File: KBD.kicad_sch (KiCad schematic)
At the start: 41 parts, among them SW1 SW_Push, SW10 SW_Push, SW11 SW_Push, SW12 SW_Push, SW13 SW_Push, SW14 SW_Push, SW15 SW_Push, SW16 SW_Push, SW17 SW_Push, SW18 SW_Push, SW2 SW_Push, SW3 SW_Push, SW4 SW_Push, SW5 SW_Push, SW6 SW_Push, SW7 SW_Push, SW8 SW_Push, SW9 SW_Push, U1 SeeeduinoXIAO

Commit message: aaaaaaa
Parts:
- removed R1, R2, R3, R4: 10k, Resistor_SMD:R_0805_2012Metric_Pad1.20x1.40mm_HandSolder, symbol Device:R
- SW1, SW10, SW11, SW12, SW13, SW14, SW15, SW16, SW17, SW18, SW2, SW3, SW4, SW5, SW6, SW7, SW8, SW9: footprint CustomKeyboard:Choc_reversible -> Split_footprints:Choc_reversible_17mmOutline
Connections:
- net Row_1: now also D1.1 (K), D13.1 (K), D16.1 (K), D5.1 (K), D9.1 (K)
- net Row_2: now also D10.1 (K), D14.1 (K), D17.1 (K), D2.1 (K), D6.1 (K)
- net Row_3: now also D11.1 (K), D15.1 (K), D18.1 (K), D3.1 (K), D7.1 (K)
- net Row_4: now also D12.1 (K), D4.1 (K), D8.1 (K)

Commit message: bbbbb
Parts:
- renumbered D17 to D10, D3 to D11, D7 to D12, D11 to D13, D15 to D14, D18 to D15, D4 to D16, D8 to D17, D12 to D18, D5 to D2, D9 to D3, D13 to D4, D16 to D5, D2 to D6, D6 to D7, D10 to D8, D14 to D9, SW17 to SW10, SW3 to SW11, SW7 to SW12, SW11 to SW13, SW15 to SW14, SW18 to SW15, SW4 to SW16, SW8 to SW17, SW12 to SW18, SW5 to SW2, SW9 to SW3, SW13 to SW4, SW16 to SW5, SW2 to SW6, SW6 to SW7, SW10 to SW8, SW14 to SW9

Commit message: bbbbbb1
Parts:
- added D19: WS2812B, LED_SMD:LED_WS2812B_PLCC4_5.0x5.0mm_P3.2mm, symbol LED:WS2812B
- added J1, J2: Conn_01x07, Connector_Hirose:Hirose_DF13-07P-1.25DS_1x07_P1.25mm_Horizontal, symbol Connector_Generic:Conn_01x07
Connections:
- net Column_1: now also J1.6 (Pin_6); no longer U1.6 (PA9_A5_D5_SCL)
- net Column_2: now also J2.1 (Pin_1); no longer U1.7 (PB08_A6_D6_TX)
- net Column_3: now also J2.2 (Pin_2); no longer U1.8 (PB09_A7_D7_RX)
- net Column_4: now also J2.3 (Pin_3); no longer U1.9 (PA7_A8_D8_SCK)
- net Column_5: now also J2.4 (Pin_4); no longer U1.10 (PA5_A9_D9_MISO)
- net Row_1: now also J1.1 (Pin_1); no longer U1.1 (PA02_A0_D0)
- net Row_2: now also J1.2 (Pin_2); no longer U1.2 (PA4_A1_D1)
- net Row_3: now also J1.3 (Pin_3); no longer U1.3 (PA10_A2_D2)
- net Row_4: now also J1.4 (Pin_4); no longer U1.4 (PA11_A3_D3)
- new net 0V: D19.3 (VSS), J2.6 (Pin_6)
- new net 5V: D19.1 (VDD), J2.7 (Pin_7)
- new net Led_In: D19.4 (DIN), J1.5 (Pin_5)
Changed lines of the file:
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@@
     (stroke (width 0) (type default))
   )
-  (global_label "Column_1" (shape output) (at 40.64 74.93 180) (fields_autoplaced)
-    (effects (font (size 1.27 1.27)) (justify right))
-    (property "Intersheetrefs" "${INTERSHEET_REFS}" (at 28.974 74.8506 0)
-      (effects (font (size 1.27 1.27)) (justify right) hide)
-    )
-  )
-  (global_label "Row_1" (shape input) (at 40.64 55.88 180) (fields_autoplaced)
-    (effects (font (size 1.27 1.27)) (justify right))
-    (property "Intersheetrefs" "${INTERSHEET_REFS}" (at 32.3002 55.8006 0)
+  (global_label "5V" (shape input) (at 55.88 130.81 90) (fields_autoplaced)
+    (effects (font (size 1.27 1.27)) (justify left))
+    (property "Intersheetrefs" "${INTERSHEET_REFS}" (at 55.88 125.6061 90)
+      (effects (font (size 1.27 1.27)) (justify left) hide)
+    )
+  )
+  (global_label "0V" (shape input) (at 71.12 107.95 0) (fields_autoplaced)
+    (effects (font (size 1.27 1.27)) (justify left))
+    (property "Intersheetrefs" "${INTERSHEET_REFS}" (at 76.3239 107.95 0)
+      (effects (font (size 1.27 1.27)) (justify left) hide)
+    )
+  )
+  (global_label "Column_1" (shape output) (at 43.18 118.11 180) (fields_autoplaced)
+    (effects (font (size 1.27 1.27)) (justify right))
+    (property "Intersheetrefs" "${INTERSHEET_REFS}" (at 31.514 118.0306 0)
+      (effects (font (size 1.27 1.27)) (justify right) hide)
+    )
+  )
+  (global_label "Row_1" (shape input) (at 43.18 105.41 180) (fields_autoplaced)
+    (effects (font (size 1.27 1.27)) (justify right))
+    (property "Intersheetrefs" "${INTERSHEET_REFS}" (at 34.8402 105.3306 0)
       (effects (font (size 1.27 1.27)) (justify right) hide)
     )
@@
     )
   )
-  (global_label "Row_2" (shape input) (at 40.64 59.69 180) (fields_autoplaced)
-    (effects (font (size 1.27 1.27)) (justify right))
-    (property "Intersheetrefs" "${INTERSHEET_REFS}" (at 32.3002 59.6106 0)
-      (effects (font (size 1.27 1.27)) (justify right) hide)
-    )
-  )
-  (global_label "Column_4" (shape output) (at 82.55 74.93 0) (fields_autoplaced)
-    (effects (font (size 1.27 1.27)) (justify left))
-    (property "Intersheetrefs" "${INTERSHEET_REFS}" (at 94.216 74.8506 0)
-      (effects (font (size 1.27 1.27)) (justify left) hide)
+  (global_label "Row_2" (shape input) (at 43.18 107.95 180) (fields_autoplaced)
+    (effects (font (size 1.27 1.27)) (justify right))
+    (property "Intersheetrefs" "${INTERSHEET_REFS}" (at 34.8402 107.8706 0)
+      (effects (font (size 1.27 1.27)) (justify right) hide)
+    )
+  )
+  (global_label "Column_4" (shape output) (at 71.12 115.57 0) (fields_autoplaced)
+    (effects (font (size 1.27 1.27)) (justify left))
+    (property "Intersheetrefs" "${INTERSHEET_REFS}" (at 82.786 115.4906 0)
+      (effects (font (size 1.27 1.27)) (justify left) hide)
+    )
+  )
+  (global_label "Led_In" (shape input) (at 43.18 115.57 180) (fields_autoplaced)
+    (effects (font (size 1.27 1.27)) (justify right))
+    (property "Intersheetrefs" "${INTERSHEET_REFS}" (at 34.2871 115.57 0)
+      (effects (font (size 1.27 1.27)) (justify right) hide)
     )
   )
@@
     )
   )
-  (global_label "Row_3" (shape input) (at 40.64 63.5 180) (fields_autoplaced)
-    (effects (font (size 1.27 1.27)) (justify right))
-    (property "Intersheetrefs" "${INTERSHEET_REFS}" (at 32.3002 63.4206 0)
-      (effects (font (size 1.27 1.27)) (justify right) hide)
-    )
-  )
-  (global_label "Column_2" (shape output) (at 40.64 78.74 180) (fields_autoplaced)
-    (effects (font (size 1.27 1.27)) (justify right))
-    (property "Intersheetrefs" "${INTERSHEET_REFS}" (at 28.974 78.6606 0)
-      (effects (font (size 1.27 1.27)) (justify right) hide)
-    )
-  )
-  (global_label "Row_4" (shape input) (at 40.64 67.31 180) (fields_autoplaced)
-    (effects (font (size 1.27 1.27)) (justify right))
-    (property "Intersheetrefs" "${INTERSHEET_REFS}" (at 32.3002 67.2306 0)
-      (effects (font (size 1.27 1.27)) (justify right) hide)
-    )
-  )
-  (global_label "Column_5" (shape output) (at 82.55 71.12 0) (fields_autoplaced)
-    (effects (font (size 1.27 1.27)) (justify left))
-    (property "Intersheetrefs" "${INTERSHEET_REFS}" (at 94.216 71.0406 0)
+  (global_label "Row_3" (shape input) (at 43.18 110.49 180) (fields_autoplaced)
+    (effects (font (size 1.27 1.27)) (justify right))
+    (property "Intersheetrefs" "${INTERSHEET_REFS}" (at 34.8402 110.4106 0)
+      (effects (font (size 1.27 1.27)) (justify right) hide)
+    )
+  )
+  (global_label "Column_2" (shape output) (at 71.12 120.65 0) (fields_autoplaced)
+    (effects (font (size 1.27 1.27)) (justify left))
+    (property "Intersheetrefs" "${INTERSHEET_REFS}" (at 83.2784 120.65 0)
+      (effects (font (size 1.27 1.27)) (justify left) hide)
+    )
+  )
+  (global_label "Row_4" (shape input) (at 43.18 113.03 180) (fields_autoplaced)
+    (effects (font (size 1.27 1.27)) (justify right))
+    (property "Intersheetrefs" "${INTERSHEET_REFS}" (at 34.8402 112.9506 0)
+      (effects (font (size 1.27 1.27)) (justify right) hide)
+    )
+  )
+  (global_label "Column_5" (shape output) (at 71.12 113.03 0) (fields_autoplaced)
+    (effects (font (size 1.27 1.27)) (justify left))
+    (property "Intersheetrefs" "${INTERSHEET_REFS}" (at 82.786 112.9506 0)
       (effects (font (size 1.27 1.27)) (justify left) hide)
     )
@@
     )
   )
-  (global_label "Column_3" (shape output) (at 82.55 78.74 0) (fields_autoplaced)
-    (effects (font (size 1.27 1.27)) (justify left))
-    (property "Intersheetrefs" "${INTERSHEET_REFS}" (at 94.216 78.6606 0)
+  (global_label "Column_3" (shape output) (at 71.12 118.11 0) (fields_autoplaced)
+    (effects (font (size 1.27 1.27)) (justify left))
+    (property "Intersheetrefs" "${INTERSHEET_REFS}" (at 82.786 118.0306 0)
       (effects (font (size 1.27 1.27)) (justify left) hide)
     )
@@
     )
   )
+  (global_label "5V" (shape input) (at 71.12 105.41 0) (fields_autoplaced)
+    (effects (font (size 1.27 1.27)) (justify left))
+    (property "Intersheetrefs" "${INTERSHEET_REFS}" (at 76.3239 105.41 0)
+      (effects (font (size 1.27 1.27)) (justify left) hide)
+    )
+  )
+  (global_label "0V" (shape input) (at 55.88 146.05 270) (fields_autoplaced)
+    (effects (font (size 1.27 1.27)) (justify right))
+    (property "Intersheetrefs" "${INTERSHEET_REFS}" (at 55.88 151.2539 90)
+      (effects (font (size 1.27 1.27)) (justify right) hide)
+    )
+  )
   (global_label "Column_2" (shape output) (at 154.94 62.23 90) (fields_autoplaced)
     (effects (font (size 1.27 1.27)) (justify left))
     (property "Intersheetrefs" "${INTERSHEET_REFS}" (at 154.8606 50.564 90)
       (effects (font (size 1.27 1.27)) (justify left) hide)
+    )
+  )
+  (global_label "Led_In" (shape input) (at 48.26 138.43 180) (fields_autoplaced)
+    (effects (font (size 1.27 1.27)) (justify right))
+    (property "Intersheetrefs" "${INTERSHEET_REFS}" (at 39.3671 138.43 0)
+      (effects (font (size 1.27 1.27)) (justify right) hide)
     )
   )
@@
     )
   )
+  (symbol (lib_id "LED:WS2812B") (at 55.88 138.43 0) (unit 1)
+    (in_bom yes) (on_board yes) (dnp no) (fields_autoplaced)
+    (property "Reference" "D19" (at 67.31 134.5439 0)
+      (effects (font (size 1.27 1.27)) hide)
+    )
+    (property "Value" "WS2812B" (at 67.31 137.0839 0)
+      (effects (font (size 1.27 1.27)) hide)
+    )
+    (property "Footprint" "LED_SMD:LED_WS2812B_PLCC4_5.0x5.0mm_P3.2mm" (at 57.15 146.05 0)
+      (effects (font (size 1.27 1.27)) (justify left top) hide)
+    )
+    (property "Datasheet" "https://cdn-shop.adafruit.com/datasheets/WS2812B.pdf" (at 58.42 147.955 0)
+      (effects (font (size 1.27 1.27)) (justify left top) hide)
+    )
+    (pin "1")
+    (pin "2")
+    (pin "3")
+    (pin "4")
+    (instances
+      (project "KBD"
+        (path "/55f2016c-a3c8-4668-bcda-098c018a0472"
+          (reference "D19") (unit 1)
+        )
+      )
+    )
+  )
   (symbol (lib_id "Switch:SW_Push") (at 167.64 124.46 0) (unit 1)
     (in_bom yes) (on_board yes) (dnp no)
@@
         )
       )
+    )
+  )
+  (symbol (lib_id "Connector_Generic:Conn_01x07") (at 48.26 113.03 0) (unit 1)
+    (in_bom yes) (on_board yes) (dnp no) (fields_autoplaced)
+    (property "Reference" "J1" (at 50.8 111.76 0)
+      (effects (font (size 1.27 1.27)) (justify left))
+    )
+    (property "Value" "Conn_01x07" (at 50.8 114.3 0)
+      (effects (font (size 1.27 1.27)) (justify left))
+    )
+    (property "Footprint" "Connector_Hirose:Hirose_DF13-07P-1.25DS_1x07_P1.25mm_Horizontal" (at 48.26 113.03 0)
+      (effects (font (size 1.27 1.27)) hide)
+    )
+    (property "Datasheet" "~" (at 48.26 113.03 0)
+      (effects (font (size 1.27 1.27)) hide)
+    )
+    (pin "1")
+    (pin "2")
+    (pin "3")
+    (pin "4")
+    (pin "5")
+    (pin "6")
+    (pin "7")
+    (instances
+      (project "KBD"
+        (path "/55f2016c-a3c8-4668-bcda-098c018a0472"
+          (reference "J1") (unit 1)
+        )
+      )
+    )
+  )
+  (symbol (lib_id "Connector_Generic:Conn_01x07") (at 66.04 113.03 180) (unit 1)
+    (in_bom yes) (on_board yes) (dnp no) (fields_autoplaced)
+    (property "Reference" "J2" (at 66.04 99.06 0)
+      (effects (font (size 1.27 1.27)))
+    )
+    (property "Value" "Conn_01x07" (at 66.04 101.6 0)
+      (effects (font (size 1.27 1.27)))
+    )
+    (property "Footprint" "Connector_Hirose:Hirose_DF13-07P-1.25DS_1x07_P1.25mm_Horizontal" (at 66.04 113.03 0)
+      (effects (font (size 1.27 1.27)) hide)
+    )
+    (property "Datasheet" "~" (at 66.04 113.03 0)
+      (effects (font (size 1.27 1.27)) hide)
+    )
+    (pin "1")
+    (pin "2")
+    (pin "3")
+    (pin "4")
+    (pin "5")
+    (pin "6")
+    (pin "7")
+    (instances
+      (project "KBD"
+        (path "/55f2016c-a3c8-4668-bcda-098c018a0472"
+          (reference "J2") (unit 1)
+        )
+      )

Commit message: bbbbbb2
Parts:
- added D20: WS2812B, LED_SMD:LED_WS2812B_PLCC4_5.0x5.0mm_P3.2mm, symbol LED:WS2812B
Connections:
- net 0V: now also D20.3 (VSS)
- net 5V: now also D20.1 (VDD)
- net at D19.2 (DOUT): now also D20.4 (DIN)
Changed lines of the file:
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@@
+    )
+  )
+  (global_label "0V" (shape input) (at 71.12 146.05 270) (fields_autoplaced)
+    (effects (font (size 1.27 1.27)) (justify right))
+    (property "Intersheetrefs" "${INTERSHEET_REFS}" (at 71.12 151.2539 90)
+      (effects (font (size 1.27 1.27)) (justify right) hide)
     )
   )
@@
     (effects (font (size 1.27 1.27)) (justify left))
     (property "Intersheetrefs" "${INTERSHEET_REFS}" (at 82.786 118.0306 0)
+      (effects (font (size 1.27 1.27)) (justify left) hide)
+    )
+  )
+  (global_label "5V" (shape input) (at 71.12 130.81 90) (fields_autoplaced)
+    (effects (font (size 1.27 1.27)) (justify left))
+    (property "Intersheetrefs" "${INTERSHEET_REFS}" (at 71.12 125.6061 90)
       (effects (font (size 1.27 1.27)) (justify left) hide)
     )
@@
         )
       )
+    )
+  )
+  (symbol (lib_id "LED:WS2812B") (at 71.12 138.43 0) (unit 1)
+    (in_bom yes) (on_board yes) (dnp no) (fields_autoplaced)
+    (property "Reference" "D20" (at 82.55 134.5439 0)
+      (effects (font (size 1.27 1.27)) hide)
+    )
+    (property "Value" "WS2812B" (at 82.55 137.0839 0)
+      (effects (font (size 1.27 1.27)) hide)
+    )
+    (property "Footprint" "LED_SMD:LED_WS2812B_PLCC4_5.0x5.0mm_P3.2mm" (at 72.39 146.05 0)
+      (effects (font (size 1.27 1.27)) (justify left top) hide)
+    )
+    (property "Datasheet" "https://cdn-shop.adafruit.com/datasheets/WS2812B.pdf" (at 73.66 147.955 0)
+      (effects (font (size 1.27 1.27)) (justify left top) hide)
+    )
+    (pin "1")
+    (pin "2")
+    (pin "3")
+    (pin "4")
+    (instances
+      (project "KBD"
+        (path "/55f2016c-a3c8-4668-bcda-098c018a0472"
+          (reference "D20") (unit 1)
+        )
+      )

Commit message: TRRS version
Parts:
- added R1, R2: 4.7k, Resistor_SMD:R_0805_2012Metric, symbol Device:R_Small
- added TRRS1: ~, SparkFun-Connectors:AUDIO-JACK-TRRS-SMD, symbol Connector:Conn_01x04_Pin
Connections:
- net 0V: now also TRRS1.2 (Pin_2)
- net 5V: now also R1.1, R2.1, TRRS1.1 (Pin_1)
- net Column_1: now also J1.7 (Pin_7); no longer J1.6 (Pin_6)
- net Column_2: now also J2.2 (Pin_2); no longer J2.1 (Pin_1)
- net Column_3: now also J2.3 (Pin_3); no longer J2.2 (Pin_2)
- net Column_4: now also J2.4 (Pin_4); no longer J2.3 (Pin_3)
- net Column_5: now also J2.5 (Pin_5); no longer J2.4 (Pin_4)
- net Led_In: now also J2.1 (Pin_1); no longer J1.5 (Pin_5)
- new net SCL: J1.6 (Pin_6), R1.2, R2.2, TRRS1.3 (Pin_3), TRRS1.4 (Pin_4)
- new net SDA: J1.5 (Pin_5)

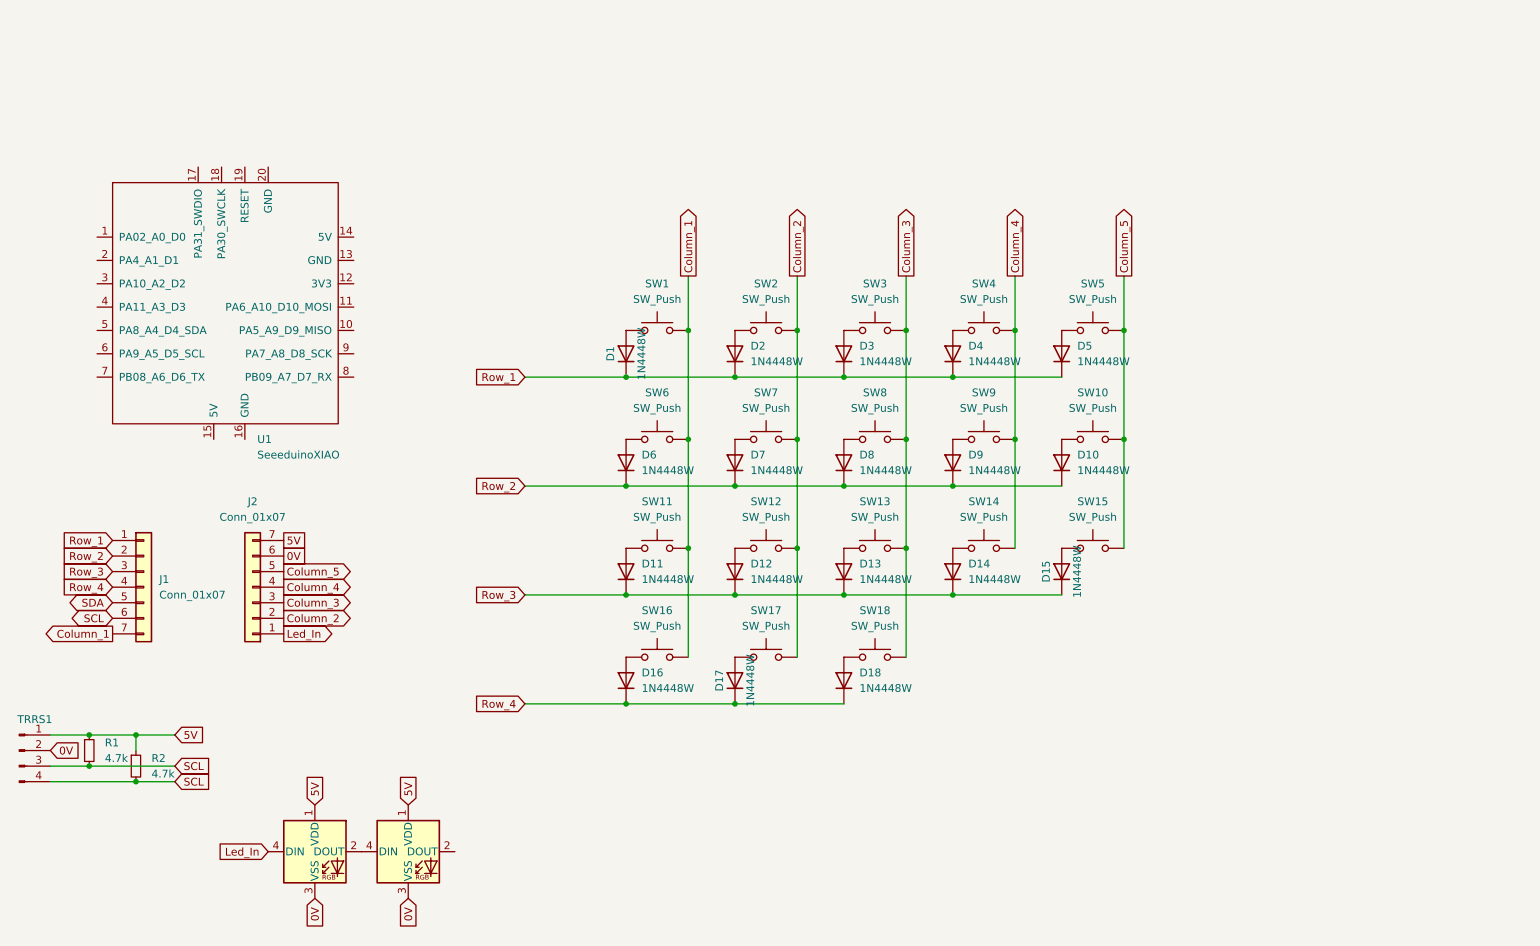
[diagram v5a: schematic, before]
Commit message: led not routed, else is done
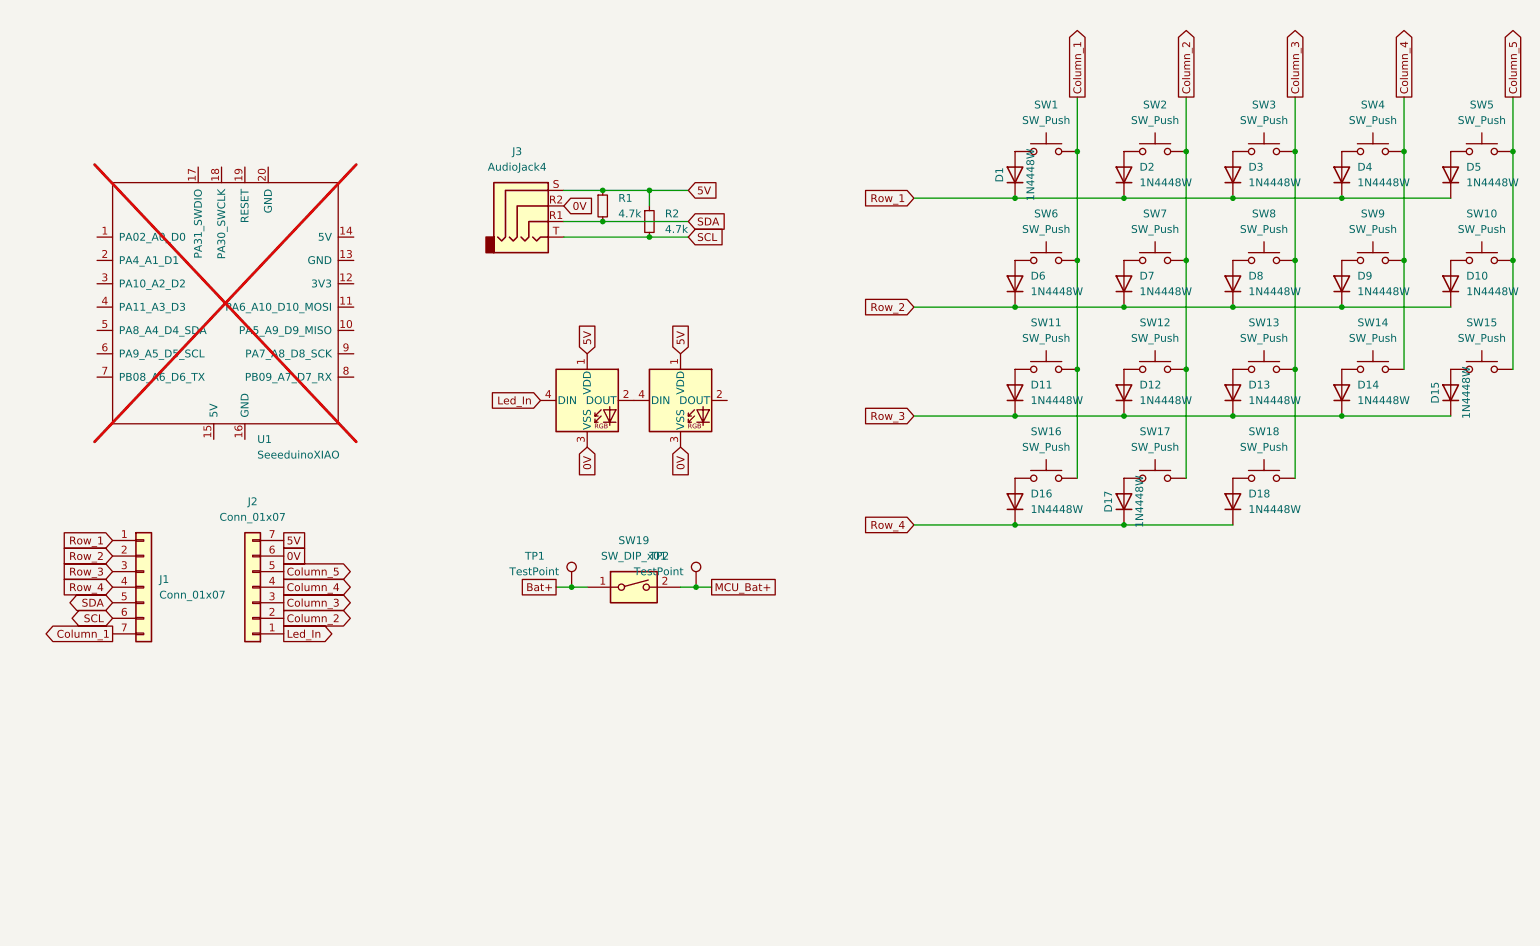
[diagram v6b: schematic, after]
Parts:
- removed TRRS1: ~, SparkFun-Connectors:AUDIO-JACK-TRRS-SMD, symbol Connector:Conn_01x04_Pin
- added J3: AudioJack4, Connector_Audio:Jack_3.5mm_PJ320D_Horizontal, symbol Connector_2:AudioJack4
- added SW19: SW_DIP_x01, Button_Switch_THT:SW_DIP_SPSTx01_Slide_6.7x4.1mm_W7.62mm_P2.54mm_LowProfile, symbol Switch:SW_DIP_x01
- added TP1, TP2: TestPoint, TestPoint:TestPoint_THTPad_2.0x2.0mm_Drill1.0mm, symbol Connector:TestPoint
- U1: now not fitted
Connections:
- net 0V: now also J3.R2
- net 5V: now also J3.S
- net SCL: now also J3.T; no longer R1.2
- net SDA: now also R1.2, J3.R1
- new net Bat+: SW19.1, TP1.1
- new net MCU_Bat+: SW19.2, TP2.1
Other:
- moved on the sheet: D1, D10, D11, D12, D13, D14, D15, D16, D17, D18, D2, D3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

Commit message: routing chaos
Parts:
- removed SW19: SW_DIP_x01, Button_Switch_THT:SW_DIP_SPSTx01_Slide_6.7x4.1mm_W7.62mm_P2.54mm_LowProfile, symbol Switch:SW_DIP_x01
- added SW19: SW_DIP_x04, Button_Switch_SMD:SW_DIP_SPSTx04_Slide_Copal_CHS-04A_W5.08mm_P1.27mm_JPin, symbol Switch:SW_DIP_x04
- added TP3, TP4, TP5: TestPoint, TestPoint:TestPoint_Pad_1.0x1.0mm, symbol Connector:TestPoint
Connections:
- net 5V: now also SW19.2, TP3.1; no longer J3.S, R1.1, R2.1
- net Bat+: now also SW19.4
- net Column_2: now also J2.1 (Pin_1); no longer J2.2 (Pin_2)
- net Column_3: now also J2.2 (Pin_2); no longer J2.3 (Pin_3)
- net Column_4: now also J2.3 (Pin_3); no longer J2.4 (Pin_4)
- net Column_5: now also J2.4 (Pin_4); no longer J2.5 (Pin_5)
- net MCU_Bat+: now also SW19.5
- net SCL: now also SW19.3
- net Led_In renamed LED_IN
- net LED_IN: now also SW19.6; no longer J2.1 (Pin_1)
- new net 3.3V: J2.5 (Pin_5), SW19.1, TP4.1
- new net I2CPullUp: J3.S, R1.1, R2.1, TP5.1
- new net LED_PWR: SW19.7, SW19.8
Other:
- moved on the sheet: TP1, TP2
